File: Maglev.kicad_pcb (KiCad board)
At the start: 4 copper layers, 265 x 130 mm, 145 parts, among them IC1 TLV1117LV33DCYR, J1 629722000214, J11 690367190672, J12 690367190672, J2 691103110002, J3 61300621121, J4 61300821121, J6 61300621121, J7 690367191672, J8 690367191672, U1 WE-TVS-82400102, U2 ESP32-C3, U4 TMAG5173A2QDBVRQ1, U5 TPS259474ARPWR, Y1 IQXC-42_830108213209

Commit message: wrong footprint on esp32 and misrouting on usb signals -> correctet error but routing needs to be adjusted
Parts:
- removed U3: ~, CUSTOM:MagnetRing
- J3: moved to F.Cu
- U2: footprint ESP32-C3FH4:QFN50P500X500X90-33N -> PCM_Espressif:QFN-32-1EP_4x4mm_P0.4mm_EP2.9x2.9mm
- moved R2 11.9 mm to (257.7, 144.4), turned to -45 degrees
- moved U1 3.20 mm to (247.9, 130.3), turned to 135 degrees
- moved C10 2.50 mm to (80.0, 100.5)
- moved J3 1.84 mm to (271.3, 108.6), turned to -11.25 degrees
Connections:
- U1 pad 2: GND -> /USB Power Circuit/USB_VBUS
- U1 pad 3: /USB_D+ -> Net-(J1-D-1)
- U1 pad 5: /USB Power Circuit/USB_VBUS -> GND
- U1 pad 6: Net-(J1-D-1) -> /USB_D+
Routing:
- net /USB Power Circuit/USB_VBUS: track 46.4 -> 28.3 mm
- net +5VP: track 43.1 -> 29.4 mm
- net Net-(J1-D+1): track 15.2 -> 2.28 mm, vias 1 -> 0
- net Net-(J1-D-1): track 15.2 -> 2.28 mm, vias 1 -> 0
- net +V_HB: track 193.1 -> 204.0 mm, vias 4 -> 7
- net /USB_D-: track 47.9 -> 40.7 mm
- net /USB_D+: track 47.6 -> 40.7 mm
- net Net-(J1-CC1): track 8.34 -> 3.99 mm
- net +3.3V: track 51.6 -> 49.1 mm, vias 40 -> 41
- net GND: track 101.8 -> 100.0 mm
- added copper zone on B.Cu, net +V_HB
- removed copper zone on In2.Cu, net +V_HB
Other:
- board text added: "Git repo"
- board text added: "←Bx"
- board text added: "↑By"
- board text added: "⊙Bz"

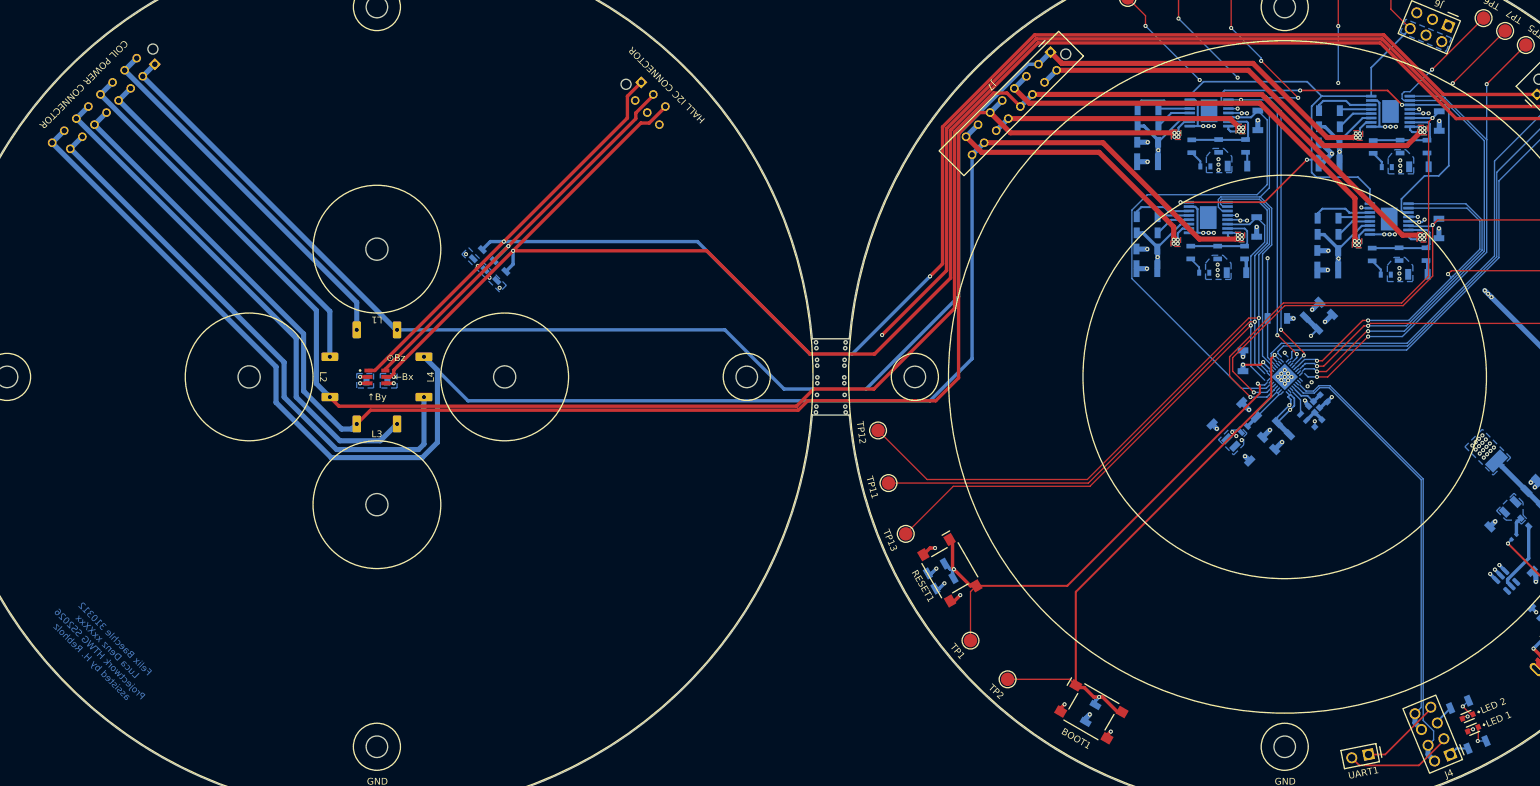
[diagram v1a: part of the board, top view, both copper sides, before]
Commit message: optimized quarz
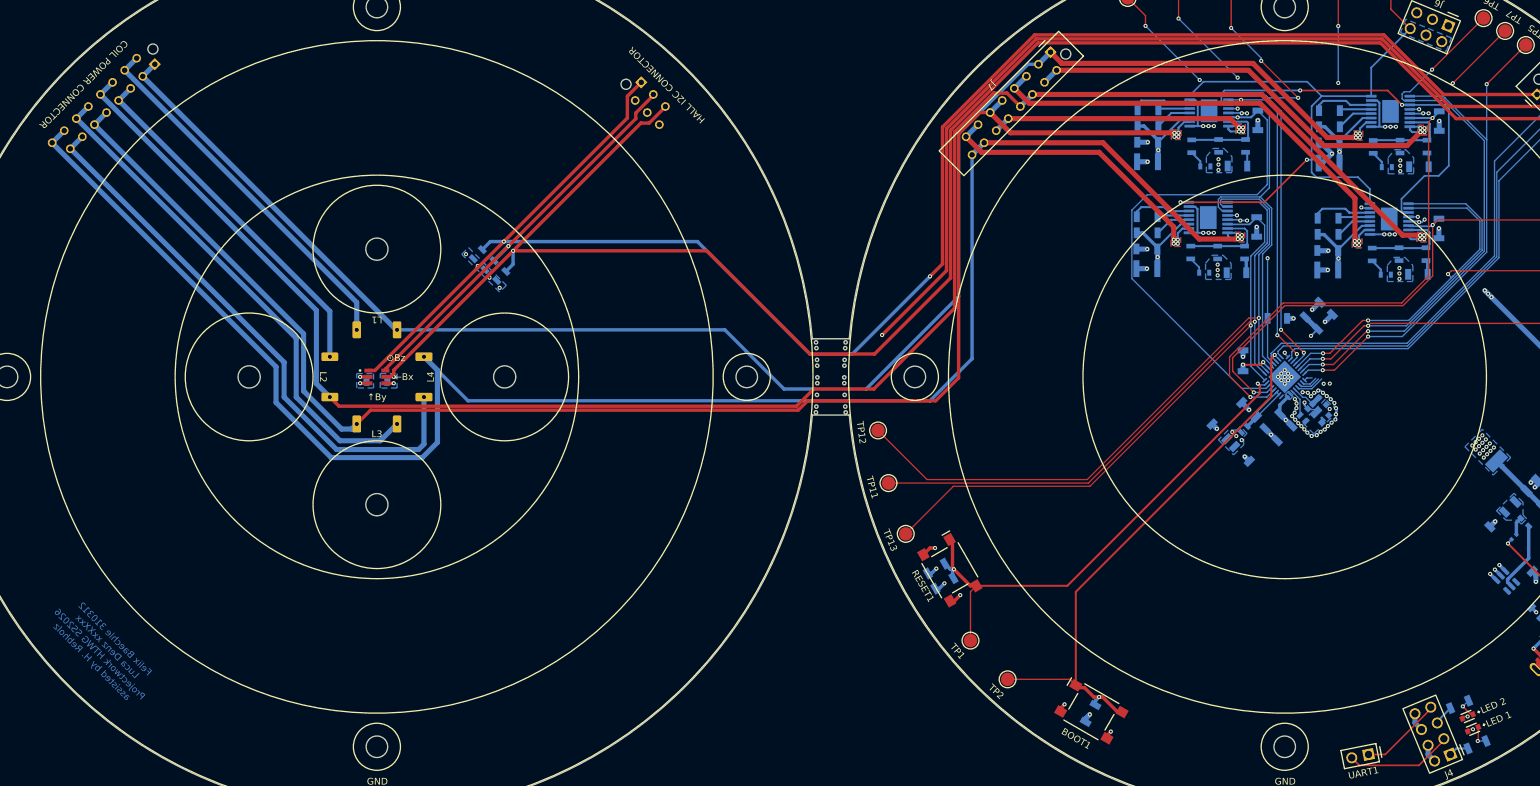
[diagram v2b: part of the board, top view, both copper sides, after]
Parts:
- added REF**: MagnetRing, CUSTOM:MagnetRing, B.Cu at (80.0, 100.0)
- U2: footprint PCM_Espressif:QFN-32-1EP_4x4mm_P0.4mm_EP2.9x2.9mm -> Package_DFN_QFN:QFN-32-1EP_5x5mm_P0.5mm_EP3.45x3.45mm
- moved C2 1.35 mm to (215.0, 108.4)
- moved C6 1.35 mm to (213.2, 106.6)
- moved C33 1.20 mm to (221.0, 106.2), turned to -135 degrees
- moved C32 0.44 mm to (220.6, 103.6)
- moved Y1 0.38 mm to (219.2, 104.8)
- moved L6 0.16 mm to (217.7, 106.1)
- moved C3 0.07 mm to (208.7, 111.5)
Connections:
- net /+XTAL_40_MHz renamed /40 MHz Oscillator/XTAL_40MHz+
- net /-XTAL_40_MHz renamed /40 MHz Oscillator/XTAL_40MHz-
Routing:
- net Net-(U2-U0RXD/GPIO20): track 68.1 -> 6.05 mm
- net Net-(U2-U0TXD/GPIO21): track 62.7 -> 7.03 mm
- net /USB_D+: track 40.7 -> 2.51 mm
- net /USB_D-: track 40.7 -> 3.75 mm
- net GND: track 100.0 -> 118.2 mm, vias 287 -> 313
- net +3.3V: track 49.1 -> 41.3 mm, vias 41 -> 40
- net Net-(C33-Pad2): track 3.24 -> 0.00 mm
- added copper zone on B.Cu, net Net-(C33-Pad2)

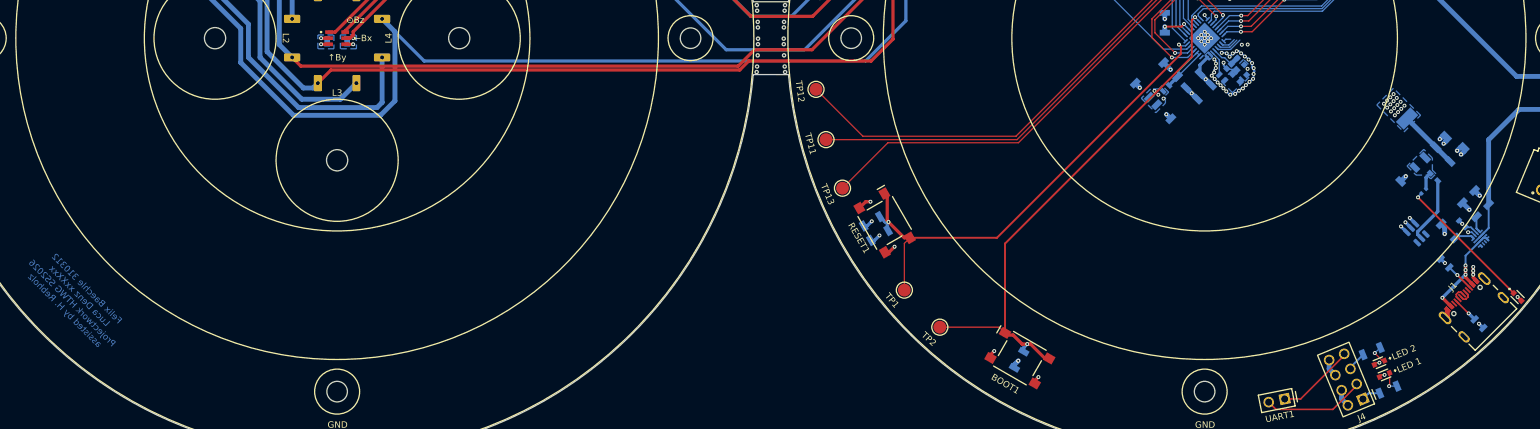
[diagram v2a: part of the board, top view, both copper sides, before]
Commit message: GND Via Stitching for Quartz
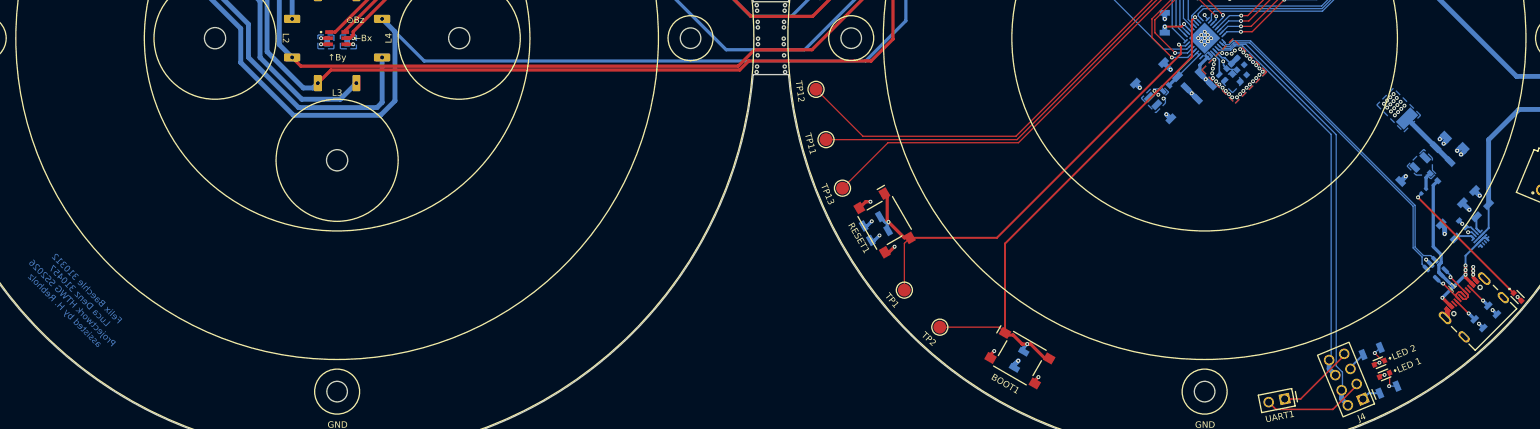
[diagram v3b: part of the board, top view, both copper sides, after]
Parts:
- moved R1 10.4 mm to (259.8, 142.3), turned to -45 degrees
- moved U1 6.38 mm to (251.0, 136.0)
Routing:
- net Net-(U2-U0RXD/GPIO20): track 6.05 -> 67.5 mm
- net Net-(U2-U0TXD/GPIO21): track 7.03 -> 62.0 mm
- net /USB_D+: track 2.51 -> 51.4 mm, vias 2 -> 0
- net /USB_D-: track 3.75 -> 51.3 mm, vias 2 -> 0
- net GND: track 118.2 -> 97.7 mm, vias 313 -> 315
- net /USB Power Circuit/USB_VBUS: track 28.3 -> 36.2 mm
- net Net-(J1-D+1): track 2.28 -> 7.03 mm, vias 0 -> 1
- net Net-(J1-D-1): track 2.28 -> 7.02 mm, vias 0 -> 1
- net Net-(J1-CC2): track 4.63 -> 3.99 mm
- added copper zone on In2.Cu, net GND
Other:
- board text added: "Felix Baechle 310312 Luca Denz 310457 Projectwork HTWG SS2026 assisted by H. Rebholz"
- board text removed: "Felix Baechle 310312 Luca Denz xxXXxx Projectwork HTWG SS2026 assisted by H. Rebholz"

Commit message: added artwork, optimized silkscreen some more
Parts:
- added G***: LOGO, Artwork:Atlas_Cu, F.Cu at (60.8, 131.7)
- added G***: LOGO, Artwork:Atlas_Mask, F.Cu at (60.8, 131.7)
- added G***: LOGO, Artwork:HTWG_EI_Logo, F.Cu at (102.0, 46.9)
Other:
- board text added: "COIL A"
- board text added: "COIL B"
- board text added: "COIL C"
- board text added: "COIL D"
- board text added: "Ringmagnet"
- board text removed: "L1"
- board text removed: "L2"
- board text removed: "L3"
- board text removed: "L4"
